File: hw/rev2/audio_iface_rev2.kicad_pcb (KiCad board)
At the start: 2 copper layers, 64 x 23 mm, 142 parts, among them J1 CONN_2, J2 CONN_2, J3 USBMICROCONN, J4 CONN_2, J5 CONN_2, J6 CONN_2, J7 CONN_2, J8 CONN_6, J9 CONN_2, U1 LT6241, U2 LTC6242, U3 AK4621, U4 K20X7_QFP64, U5 TPS61252, U6 LP2992AILD-5.0, U7 LTC6242, U8 TPA6130A2, X1 XTAL

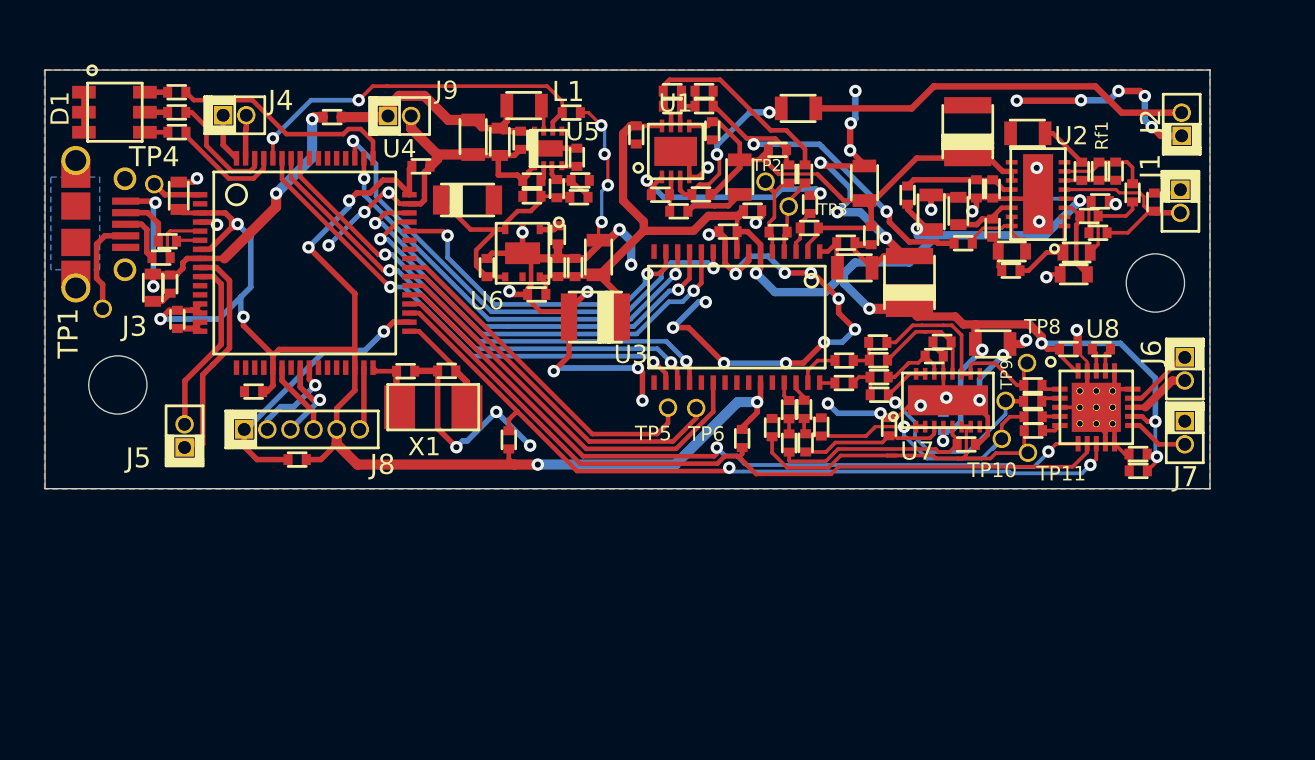
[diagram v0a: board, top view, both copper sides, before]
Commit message: Added extra oscillator JIC. Moved labels and made it pretty. Also fixed a missing capacitron
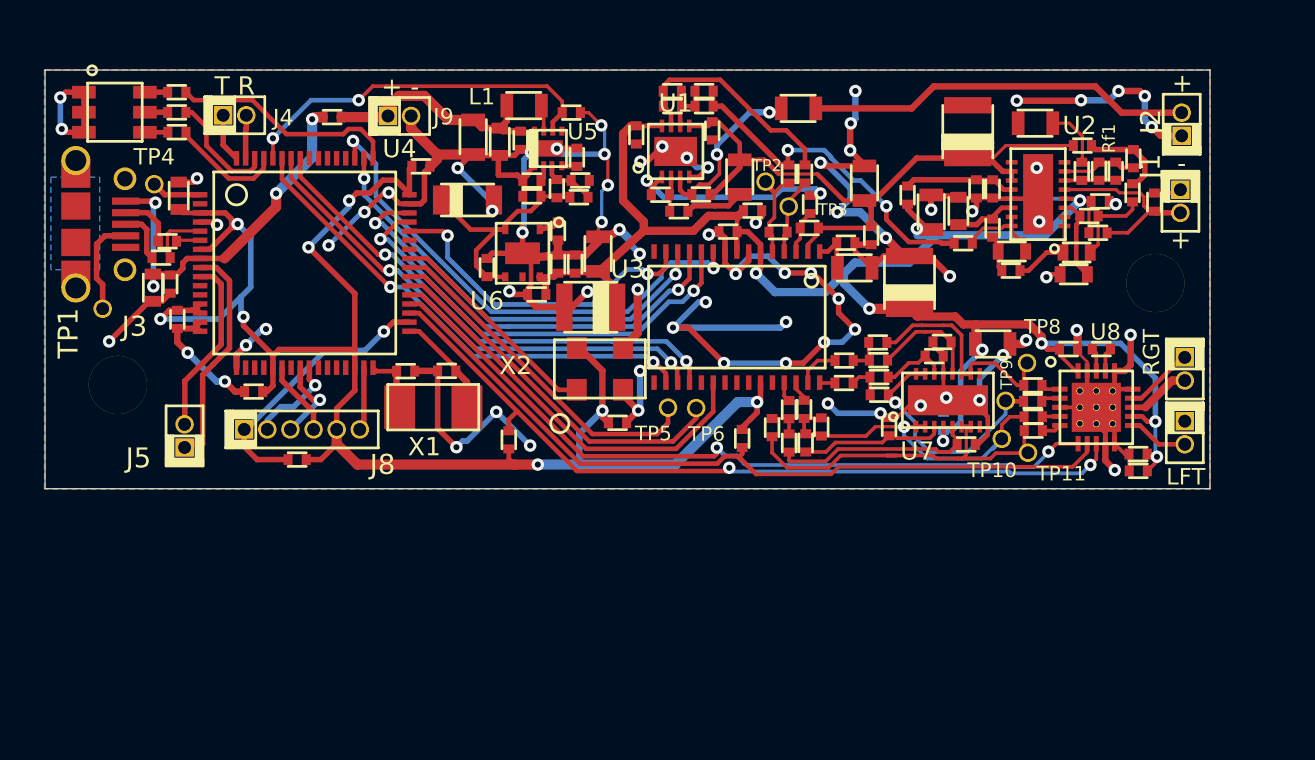
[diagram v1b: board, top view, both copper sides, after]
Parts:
- added C70: 0.01u, SMD0402, F.Cu at (211.8, 76.9)
- added C71: 10n, SMD0402, F.Cu at (183.4, 91.4)
- added X2: ASFLM2-12.288MHZ, ASFLM, F.Cu at (182.5, 88.4)
- D1: value LED3 -> LTST-C19FD1WT
- moved R15 16.8 mm to (209.0, 76.2)
- moved G*** 1.29 mm to (179.3, 77.4)
- moved C2 0.70 mm to (206.4, 74.9)
- moved C19 0.60 mm to (182.0, 85.0)
- moved C45 0.21 mm to (180.2, 80.8)
- moved C49 0.19 mm to (182.4, 82.1)
- moved C48 0.19 mm to (181.1, 82.7)
- moved C46 0.19 mm to (180.2, 82.7)
- renumbered J7 to LFT, VAL to OSHW, J6 to RGT
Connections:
- C16 pad 2: N-0000053 (its old number) -> N-0000052
- C20 pad 1: N-0000053 (its old number) -> N-0000052
- C3 pad 2: N-0000039 (its old number) -> N-0000042
- R13 pad 1: N-0000053 (its old number) -> N-0000052
- R15 pad 1: N-0000053 (its old number) -> N-0000045
- R18 pad 1: N-0000053 (its old number) -> N-0000052
- R7 pad 1: N-0000039 (its old number) -> N-0000045
- Rf1 pad 2: N-0000039 (its old number) -> N-0000042
- U2 pad o2: N-0000039 (its old number) -> N-0000042
- U4 pad 41: (no net) -> N-00000111
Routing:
- net AGND_IN: track 212.2 -> 253.2 mm, vias 58 -> 75
- net N-0000053 (its old number): track 20.6 -> 0.00 mm, vias 2 -> 0
- net N-0000052: track 0.00 -> 18.9 mm, vias 0 -> 2
- net N-00000111: track 0.00 -> 12.2 mm
- net +3V: track 82.2 -> 90.6 mm, vias 7 -> 8
- net N-0000039 (its old number): track 5.04 -> 0.00 mm
- net N-0000045: track 0.00 -> 4.92 mm
- net N-0000042: track 0.00 -> 4.20 mm
- net /Microcontroller/CODEC_MCLK: track 28.1 -> 32.1 mm, vias 2 -> 3
- net VCOM_VRT: track 33.9 -> 36.9 mm
- net N-0000041: track 2.67 -> 3.37 mm
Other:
- board text added: "+"
- board text added: "+ -"
- board text added: "-"
- board text added: "T R"
- board text removed: "Add 12.288!"

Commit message: rev2a finalized
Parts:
- G***: moved to F.Cu
- moved R20 4.49 mm to (161.4, 92.8), turned to 270 degrees
- moved G*** 0.47 mm to (179.1, 77.9)
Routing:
- net AGND_IN: track 253.2 -> 261.7 mm, vias 75 -> 76
- net +3V: track 90.6 -> 95.5 mm
- net USB_5V: track 21.8 -> 24.0 mm
- net /Microcontroller/~RESET: track 15.2 -> 13.3 mm
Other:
- board text added: "3"
- board text added: "C"
- board text added: "G"
- board text added: "I"
- board text added: "O"
- board text added: "R"

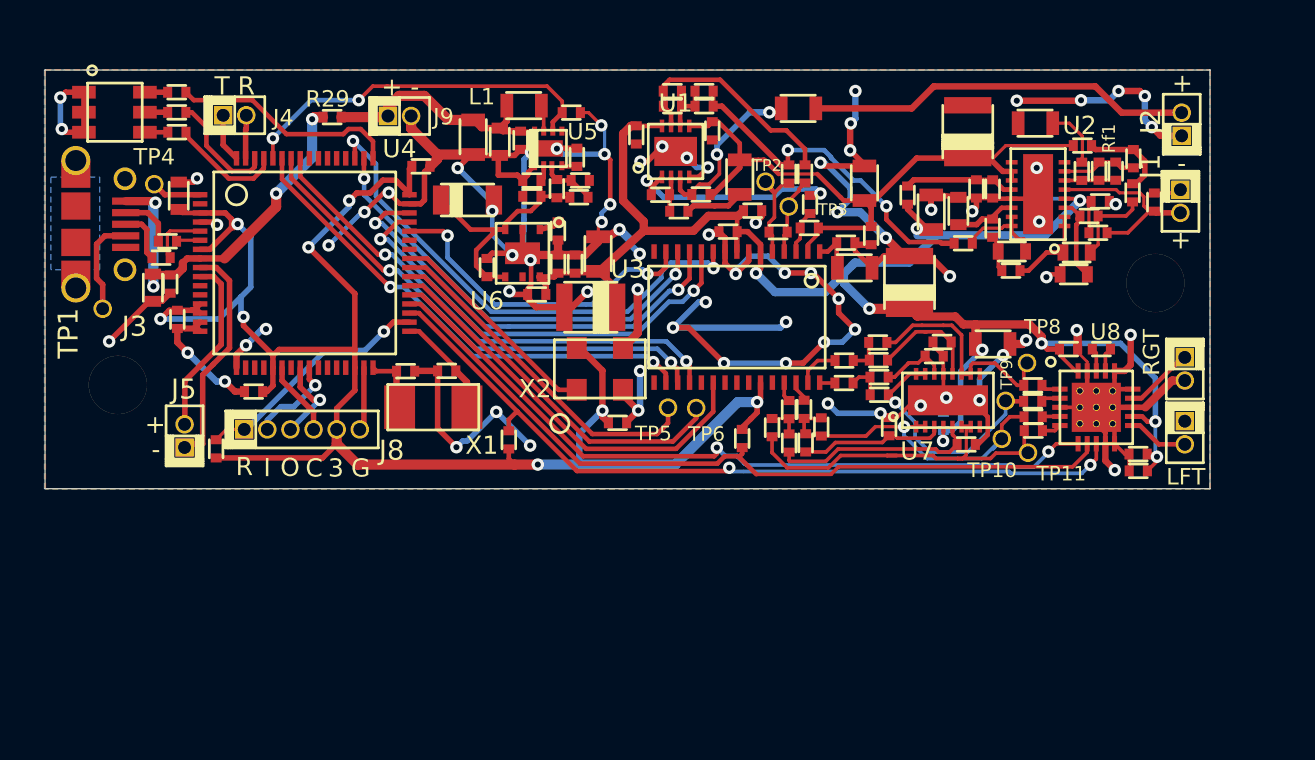
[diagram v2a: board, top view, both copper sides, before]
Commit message: Rev 2a sent off for manufacturing: Slot added instead of drill hole at audio IO end Drill added near center Fixed huge error in HP amp schematic/layout Got rid of more labels Got rid of redundant UART port. Not sure how that happened twice... Got rid of DC blocking before CODEC inputs
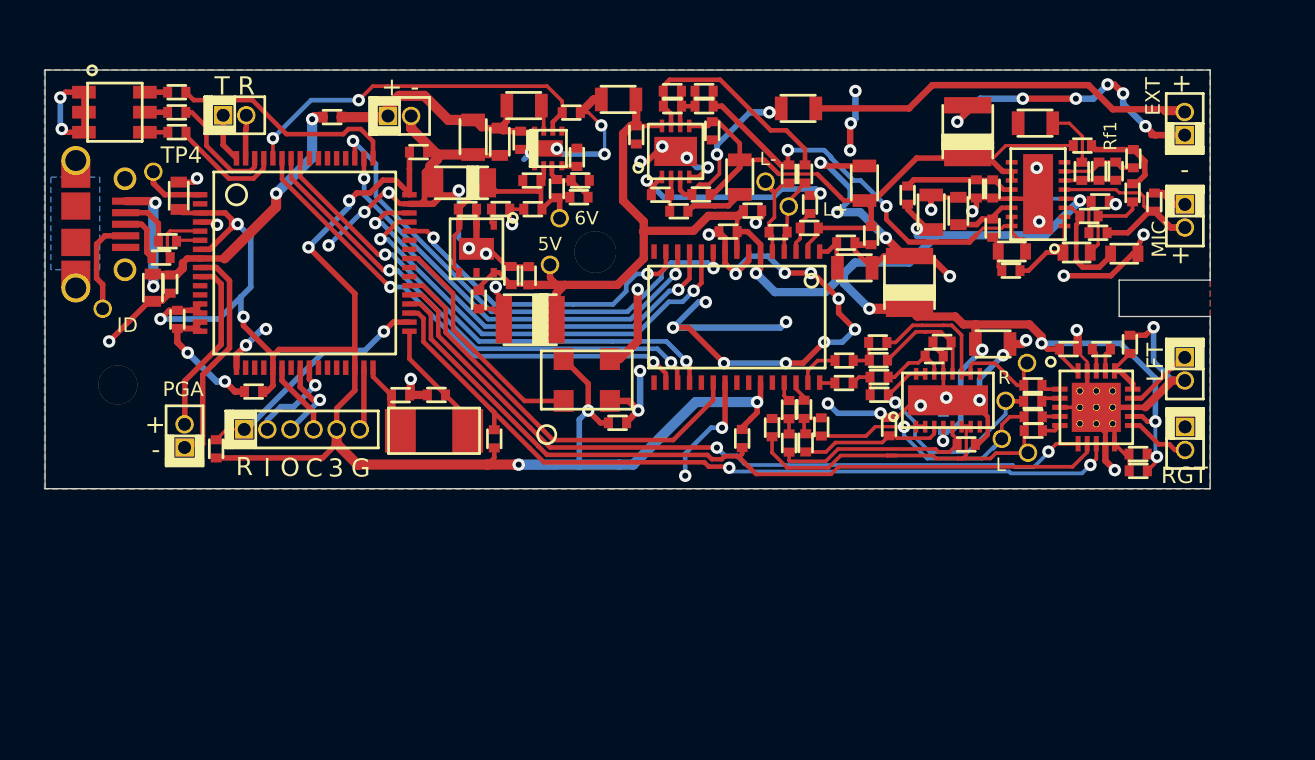
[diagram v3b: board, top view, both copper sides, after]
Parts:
- removed C16: 1u, SMD0402
- added C72: 1u, SMD0402, F.Cu at (211.6, 87.1)
- L1: value 1.5u -> MLZ2012A1R5WT000
- TP5: value TP_PTB3 -> TP
- TP6: value TP_PTB16 -> TP
- moved SCREW_HOLE_2-56 30.8 mm to (182.2, 82.0)
- moved TP6 12.8 mm to (180.3, 80.1)
- moved TP5 10.2 mm to (179.7, 82.7)
- moved C49 8.57 mm to (183.5, 73.6), turned to 180 degrees
- moved C48 5.64 mm to (175.8, 84.6), turned to 270 degrees
- moved C19 3.40 mm to (178.7, 85.7)
- moved C44 3.39 mm to (175.2, 79.6), turned to 180 degrees
- moved C45 3.37 mm to (177.0, 79.6), turned to 180 degrees
- moved C7 3.00 mm to (211.3, 82.1), turned to 180 degrees
- moved C46 2.65 mm to (177.6, 83.3)
- moved U6 2.54 mm to (175.7, 81.8)
- moved G*** 2.35 mm to (176.8, 77.6)
- moved C36 1.44 mm to (173.5, 89.8)
- moved C35 1.34 mm to (171.5, 89.9)
- moved X1 1.30 mm to (173.4, 91.8)
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- renumbered RGT to LFT, LFT to RGT
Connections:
- C11 pad 2: N-0000054 -> N-0000053
- C20 pad 1: N-0000052 (its old number) -> N-0000053
- R13 pad 1: N-0000052 (its old number) -> N-0000053
- R18 pad 1: N-0000052 (its old number) -> N-0000053
- TP5 pad 1: /Microcontroller/UART_TX -> +5VA
- TP6 pad 1: /Microcontroller/UART_RX -> +6V
- U2 pad n4: N-0000054 -> N-0000053
- U2 pad o4: N-0000054 -> N-0000053
- U4 pad 39: /Microcontroller/UART_RX -> (no net)
- U4 pad 40: /Microcontroller/UART_TX -> (no net)
- U8 pad 15: AGND_IN -> N-0000059
- U8 pad 16: AGND_IN -> N-0000059
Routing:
- net N-0000053: track 0.00 -> 24.7 mm, vias 0 -> 2
- net AGND_IN: track 261.7 -> 237.9 mm, vias 76 -> 70
- net /Microcontroller/UART_RX: track 20.6 -> 0.00 mm
- net /Microcontroller/UART_TX: track 19.1 -> 0.00 mm
- net N-0000052 (its old number): track 18.9 -> 0.00 mm, vias 2 -> 0
- net +5VA: track 99.5 -> 106.7 mm
- net N-0000054: track 5.05 -> 0.00 mm
- net (no net): track 0.00 -> 3.38 mm, vias 0 -> 3
- net /Audio In/MIC_IN: track 10.3 -> 13.2 mm
- net N-0000059: track 0.00 -> 2.90 mm
- net /Audio In/EXT_IN: track 21.2 -> 22.6 mm
- net N-0000046: track 4.79 -> 6.20 mm
- net /Microcontroller/CODEC_MCLK: track 32.1 -> 33.3 mm
- net N-0000092: track 5.79 -> 6.80 mm
- net N-0000084: track 2.76 -> 3.46 mm
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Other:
- outline, holes or cut-outs redrawn
- board text added: "5V"
- board text added: "6V"
- board text added: "AudioPulse rev2b 2014"
- board text added: "EXT"
- board text added: "ID"
- board text added: "L"
- board text added: "L+"
- board text added: "L-"
- board text added: "MIC"
- board text added: "PGA"
- board text removed: "AudioPulse rev2a 2014"

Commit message: Added serial flash module to schematic and began layout
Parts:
- added C16: 0.1u, SMD0402, F.Cu at (216.0, 95.0)
- added C73: 1u, SMD0402, F.Cu at (216.0, 95.0)
- added U9: MT29FXX01A, MICRON_VFBGA63, B.Cu at (164.5, 83.0)
- R23: value RES -> 220
- R24: value RES -> 7.5
- R30: value RES -> 39
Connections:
- U4 pad 43: (no net) -> /Microcontroller/SPI1_CS_FLASH
- U4 pad 52: (no net) -> /Microcontroller/SPI1_SIN
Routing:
- net +3V: track 95.8 -> 66.6 mm, vias 8 -> 3
- net AGND_IN: track 237.9 -> 223.5 mm, vias 70 -> 63
- added copper zone on Inner1.Cu, net AGND_IN
- added copper zone on Inner2.Cu, net AGND_IN
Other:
- copper layers 2 -> 4
- rule trace_min: 0.1524 -> 0.127
- rule via_min_drill: 0.3302 -> 0.254
- rule via_min_size: 0.6858 -> 0.4572

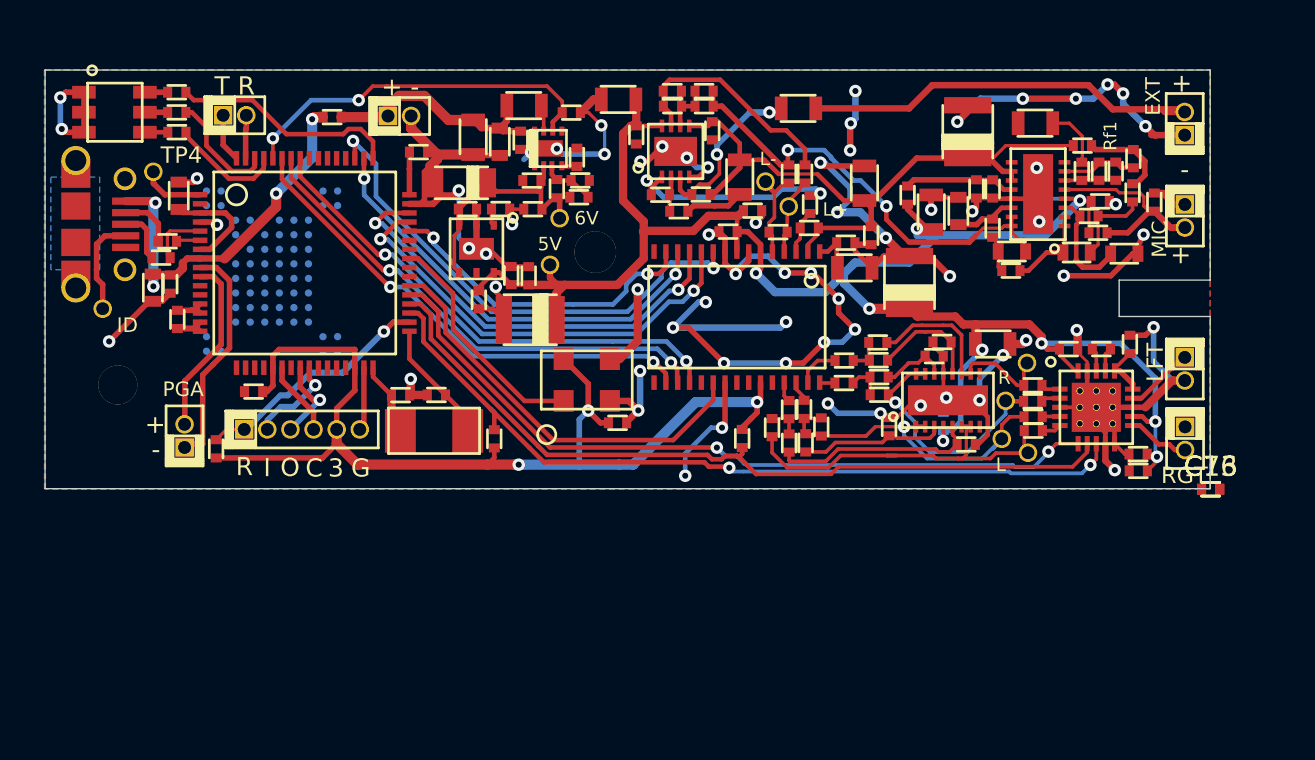
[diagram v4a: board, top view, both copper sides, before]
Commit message: Added SMA connectors, still need to recreate keepouts
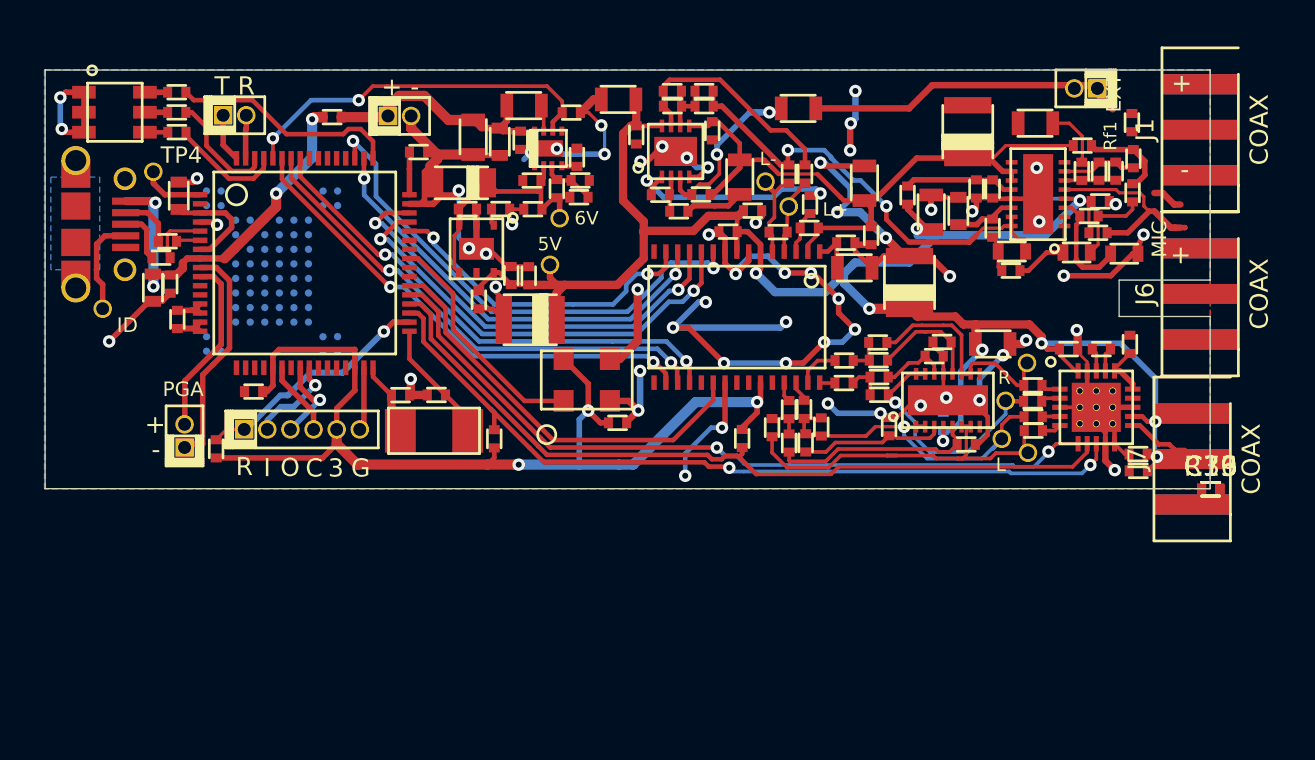
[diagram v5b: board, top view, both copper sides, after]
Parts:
- removed G***: LOGO, LOGO
- removed LFT, RGT: CONN_2, HDR_2X1_50MIL
- removed OSHW: OSHW, OSHW
- removed SCREW_HOLE_2-56 (x2): VAL**, SCREW_HOLE_2-56
- added J6: COAX, SMA_EDGE, F.Cu at (217.6, 84.3)
- added J7: COAX, SMA_EDGE, F.Cu at (217.1, 93.4)
- added R39: 100k, SMD0402, F.Cu at (216.0, 95.0)
- J1: value CONN_2 -> COAX; footprint HDR_2X1_50MIL -> SMA_EDGE
- moved J2 5.76 mm to (209.2, 73.0), turned to 180 degrees
- moved J1 5.58 mm to (217.6, 75.3), turned to 90 degrees
- moved C1 4.54 mm to (211.7, 74.9)
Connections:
- J1 pad 1: AGND_IN -> /Audio In/MIC_IN
- J1 pad 2: /Audio In/MIC_IN -> AGND_IN
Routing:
- net /Audio In/EXT_IN: track 22.6 -> 6.93 mm
- net AGND_IN: track 223.5 -> 211.7 mm, vias 63 -> 57
- net +5VA: track 106.7 -> 101.4 mm, vias 9 -> 7
- net /HP Amp/HPL: track 3.79 -> 0.00 mm
- net (no net): track 3.38 -> 5.08 mm
- net /HP Amp/HPR: track 3.44 -> 4.02 mm, vias 0 -> 1
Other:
- board text added: "AudioPulse rev3a 2015"
- board text removed: "AudioPulse rev2b 2014"

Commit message: Updated layout to what was submitted for rev3a
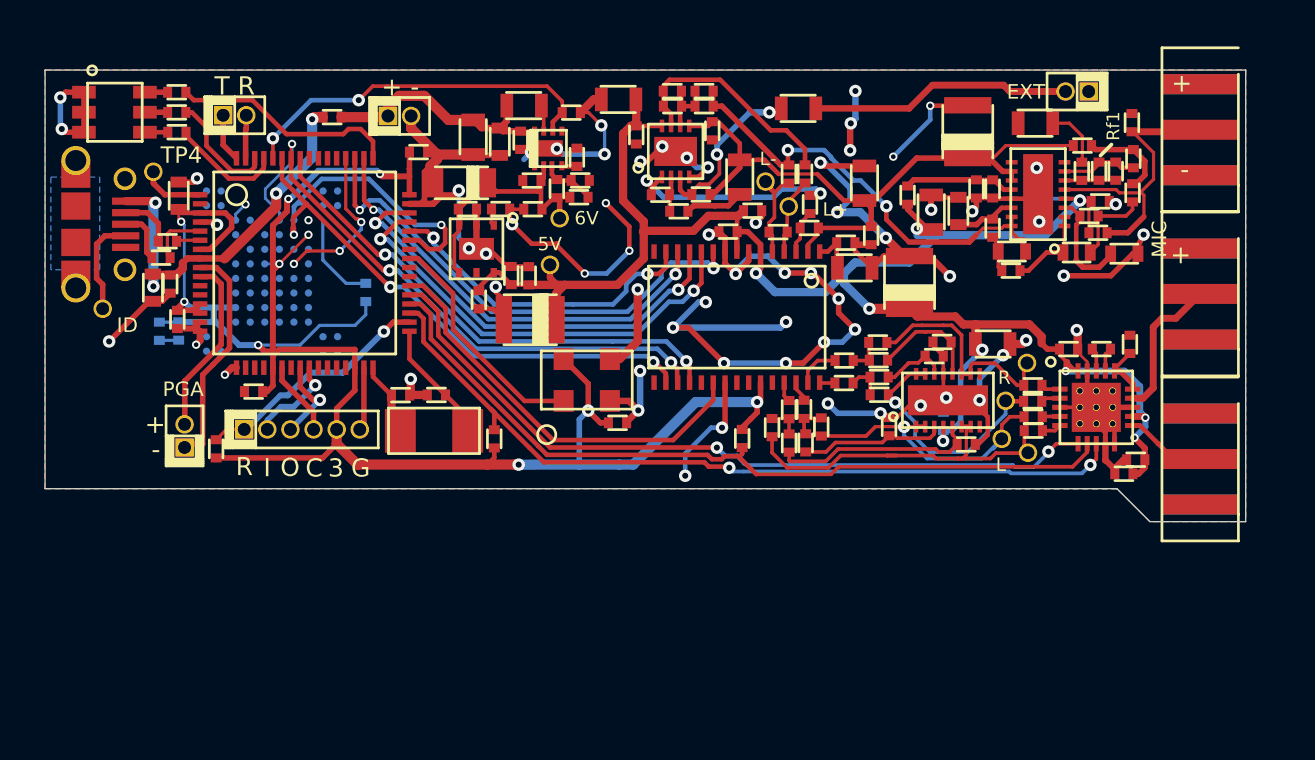
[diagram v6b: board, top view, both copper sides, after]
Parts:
- C16, C73, R39: moved to B.Cu
- moved C73 58.4 mm to (158.3, 86.3), turned to 90 degrees
- moved C16 57.4 mm to (159.3, 86.3), turned to 90 degrees
- moved R39 47.7 mm to (169.6, 84.2), turned to 270 degrees
- moved C67 0.81 mm to (211.3, 94.2)
- moved J2 0.51 mm to (208.7, 73.2)
- moved J7 0.44 mm to (217.6, 93.4)
- moved C68 0.34 mm to (211.9, 93.4)
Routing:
- net +3V: track 66.6 -> 110.3 mm, vias 3 -> 10
- net /Microcontroller/SPI1_CS_FLASH: track 0.00 -> 20.8 mm, vias 0 -> 1
- net /Microcontroller/SPI1_SIN: track 0.00 -> 8.81 mm, vias 0 -> 3
- net /HP Amp/HPL: track 0.00 -> 8.04 mm
- net /Audio In/EXT_IN: track 6.93 -> 14.4 mm
- net /Microcontroller/SPI1_SCK: track 27.4 -> 33.3 mm, vias 2 -> 3
- net AGND_IN: track 211.7 -> 216.9 mm, vias 57 -> 64
- net /Audio In/MIC_IN: track 13.2 -> 16.0 mm
- net +5VA: track 101.4 -> 103.9 mm, vias 7 -> 9
- net /Microcontroller/SPI1_SOUT: track 27.2 -> 29.2 mm, vias 2 -> 3
- net (no net): track 5.08 -> 3.38 mm
- net /Microcontroller/CODEC_MCLK: track 33.3 -> 32.8 mm
- net /HP Amp/HPR: track 4.02 -> 4.55 mm, vias 1 -> 0
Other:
- board size 64 x 23 mm -> 66 x 24.8 mm
